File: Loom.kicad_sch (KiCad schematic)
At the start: 65 parts, among them SW1 SW_Push, SW2 SW_SPST, SW3 SW_Push, SW4 SW_Push

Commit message: Add wheel speed sensors, telemetry board
TODO:
- ETC
- Relay Indicator Board
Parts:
- added TEL1: Terminal Block, symbol Connector_Generic:Conn_01x02
- added TEL2: Amphenol AT, symbol Connector_Generic:Conn_01x02
- added WSF, WSR: TE AMPSEAL, symbol Connector_Generic:Conn_01x08
- added WSF1, WSF2, WSR1, WSR2: Conn_01x02, symbol Connector_Generic:Conn_01x02
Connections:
- net CANH: now also TEL2.1 (Pin_1), WSF.3 (Pin_3), WSR.3 (Pin_3)
- net CANL: now also TEL2.2 (Pin_2), WSF.2 (Pin_2), WSR.2 (Pin_2)
- net MiscPWR: now also TEL1.1 (Pin_1), WSF.1 (Pin_1), WSR.1 (Pin_1)
- net SENGND: now also TEL1.2 (Pin_2), WSF.8 (Pin_8), WSR.8 (Pin_8)
- new net: WSR.4 (Pin_4), WSR1.1 (Pin_1)
- new net: WSR.5 (Pin_5), WSR1.2 (Pin_2)
- new net: WSR.6 (Pin_6), WSR2.1 (Pin_1)
- new net: WSR.7 (Pin_7), WSR2.2 (Pin_2)
- new net: WSF.4 (Pin_4), WSF1.1 (Pin_1)
- new net: WSF.5 (Pin_5), WSF1.2 (Pin_2)
- new net: WSF.6 (Pin_6), WSF2.1 (Pin_1)
- new net: WSF.7 (Pin_7), WSF2.2 (Pin_2)
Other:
- note added: "(12V) Power CANL CANH Sens1S Sens1G Sens2S Sens2G Gnd"
- note added: "(12V) Power Ground"
- note added: "CANH CANL"
- note added: "Telemetry"
- note added: "Wheel Speed Sensors"
- moved on the sheet: D2, FAN1, FAN2, R1, R2, SW4

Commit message: Start splitting loom into separate front/rear
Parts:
- removed APP1, APP2, BPS: Conn_01x03, symbol Connector_Generic:Conn_01x03
- removed BLS: Conn_01x03, symbol Connector_Generic:Conn_01x02
- removed BSPD: AMPSEAL (776273-1), symbol Connector_Generic:Conn_01x14
- removed BTS, INS, WSF1, WSF2: Conn_01x02, symbol Connector_Generic:Conn_01x02
- removed D1, D2: LED_Small, symbol Device:LED_Small
- removed DSH1: TE 776273-1, symbol Connector_Generic:Conn_01x14
- removed DSH2: Superseal 1.5, Connector_PinHeader_2.54mm:PinHeader_1x06_P2.54mm_Vertical, symbol Connector_Generic:Conn_01x06
- removed DSH3: No Connector, symbol Connector_Generic:Conn_01x02
- removed DSH4: Superseal 1.5, symbol Connector_Generic:Conn_01x04
- removed DSH5: JST XH2.54, symbol Connector_Generic:Conn_01x04
- removed R1, R2: R_Small, symbol Device:R_Small
- removed SW1, SW3, SW4: SW_Push, symbol Switch:SW_Push
- removed SW2: SW_SPST, symbol Switch:SW_SPST
- removed TEL1: Terminal Block, symbol Connector_Generic:Conn_01x02
- removed TEL2: Amphenol AT, symbol Connector_Generic:Conn_01x02
- removed WSF: TE AMPSEAL, symbol Connector_Generic:Conn_01x08
- added TSP: Conn_01x04, symbol Connector_Generic:Conn_01x04
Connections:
- net MiscPWR: now also LES.1 (Pin_1)
- net Front of Firewall/BLSSig: now reaches BKL.2 (Pin_2)
- net Front of Firewall/TPSPwr1: now reaches TPS.1 (Pin_1)
- net Front of Firewall/TPSGnd1: now reaches TPS.3 (Pin_3)
- net Front of Firewall/TPSPwr2: now reaches TPS.4 (Pin_4)
- net Front of Firewall/TPSSig2: now reaches TPS.5 (Pin_5)
- net Front of Firewall/TPSGnd2: now reaches TPS.6 (Pin_6)
- new net Front of Firewall/STEP-1+: TSP.1 (Pin_1)
- new net Front of Firewall/STEP-1-: TSP.2 (Pin_2)
- new net Front of Firewall/STEP-2+: TSP.3 (Pin_3)
- new net Front of Firewall/STEP-2-: TSP.4 (Pin_4)
- no-connect marks 18 -> 10
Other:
- added sheet Front of Firewall (front.kicad_sch)
- note added: "Brake Light"
- note added: "Power Box (Distribution, Fuse and Relay Boxes, Starter Relay)"
- note added: "Throttle Body"
- note removed: "(12V) Power Ground"
- note removed: "(12V) Power Neutral Shift Dn Shift Up Tacho CANL CANH ESTOP 1 2 Starter Sig Fan Sig Gnd Gnd Gnd"
- note removed: "(12V) Power Signal"
- note removed: "(5V) Power Signal Ground"
- note removed: "Brake Sensors etc."
- note removed: "CANH CANL"
- note removed: "Dash Breakout PCB"
- note removed: "Dashboard"
- note removed: "Dashboard Left"
- note removed: "Dashboard Right"
- note removed: "Dashboard Screen"
- note removed: "Disp 5V TX RX Gnd"
- note removed: "ESTOP 1 2"
- note removed: "ETC Control"
- note removed: "Launch Control Button"
- note removed: "Neutral LED+ Neutral LED- Starter 12V Starter Sig Fan Sig Gnd"
- note removed: "Power (Battery, Fuse, LVMS, Distribution/Relay/Fuse Box)"
- note removed: "Power BPS Power BPS Signal BPS Ground Ground TPS Power TPS Signal TPS Ground Ground Shutdown C Shutdown NC Shutdown NO Ground Ground"
- note removed: "Power Signal Ground"
- note removed: "TODO Control Unit"
- note removed: "Telemetry"
- note removed: "to dash estop"
- company: (none) -> Full Blue Racing
- title: (none) -> FBR25 Loom - Electrical Diagram
- moved on the sheet: BAT, BKL, FSE, LES, LVM, QS1, QS2, QS3, QS4, QSS, RES, SER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

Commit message: Remove LVMSPwr, replace with MiscPwr
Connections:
- net MiscPWR: now also RBX4.85, RBX5.85
- net LVMS 12V: no longer names the net of DBX.1 (Pin_1), DBX.2 (Pin_2), DBX.3 (Pin_3), DBX.4 (Pin_4), DBX.5 (Pin_5), DBX.6 (Pin_6), DBX.7 (Pin_7), DBX.8 (Pin_8), FBX2.1 (Pin_1), FBX2.2 (Pin_2), FBX2.3 (Pin_3), FBX2.4 (Pin_4), FBX2.5 (Pin_5), LVM.2 (Pin_2), RBX1.87, RBX2.87, RBX3.87, RBX5.87
- net LVMS 12V: no longer RBX4.85, RBX5.85
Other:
- sheet Front of Firewall ports: added none; removed LVMSPWR
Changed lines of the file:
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@@
 	)
 	(junction
-		(at 553.72 149.86)
-		(diameter 0)
-		(color 0 0 0 0)
-	)
-	(junction
 		(at 223.52 233.68)
 		(diameter 0)
@@
 	)
 	(junction
-		(at 474.98 241.3)
+		(at 292.1 93.98)
 		(diameter 0)
-		(color 255 0 0 1)
+		(color 0 0 0 0)
 	)
 	(junction
-		(at 292.1 93.98)
+		(at 474.98 317.5)
 		(diameter 0)
 		(color 0 0 0 0)
@@
 	(wire
 		(pts
-			(xy 172.72 218.44) (xy 38.1 218.44)
-		)
-		(stroke
-			(width 0)
-			(type default)
-			(color 255 0 0 1)
-		)
-	)
-	(wire
-		(pts
 			(xy 165.1 274.32) (xy 38.1 274.32)
 		)
@@
 	(wire
 		(pts
-			(xy 474.98 259.08) (xy 474.98 307.34)
-		)
-		(stroke
-			(width 0)
-			(type default)
-			(color 255 0 0 1)
-		)
-	)
-	(wire
-		(pts
 			(xy 106.68 373.38) (xy 111.76 373.38)
 		)
@@
 	(wire
 		(pts
-			(xy 474.98 149.86) (xy 474.98 241.3)
-		)
-		(stroke
-			(width 0)
-			(type default)
-			(color 255 0 0 1)
-		)
-	)
-	(wire
-		(pts
 			(xy 248.92 299.72) (xy 248.92 223.52)
 		)
@@
 	(wire
 		(pts
-			(xy 373.38 317.5) (xy 541.02 317.5)
+			(xy 373.38 317.5) (xy 474.98 317.5)
 		)
 		(stroke
@@
 	(wire
 		(pts
+			(xy 474.98 317.5) (xy 541.02 317.5)
+		)
+		(stroke
+			(width 0)
+			(type default)
+			(color 255 0 0 1)
+		)
+	)
+	(wire
+		(pts
 			(xy 203.2 25.4) (xy 132.08 25.4)
 		)
@@
 	(wire
 		(pts
-			(xy 172.72 307.34) (xy 172.72 218.44)
-		)
-		(stroke
-			(width 0)
-			(type default)
-			(color 255 0 0 1)
-		)
-	)
-	(wire
-		(pts
 			(xy 429.26 22.86) (xy 538.48 22.86)
 		)
@@
 	(wire
 		(pts
-			(xy 474.98 149.86) (xy 553.72 149.86)
-		)
-		(stroke
-			(width 0)
-			(type default)
-			(color 255 0 0 1)
-		)
-	)
-	(wire
-		(pts
 			(xy 538.48 63.5) (xy 538.48 50.8)
 		)
@@
 	(wire
 		(pts
-			(xy 474.98 307.34) (xy 172.72 307.34)
+			(xy 236.22 330.2) (xy 152.4 330.2)
 		)
 		(stroke
 			(width 0)
 			(type default)
-			(color 255 0 0 1)
 		)
 	)
 	(wire
 		(pts
-			(xy 236.22 330.2) (xy 152.4 330.2)
+			(xy 474.98 259.08) (xy 474.98 317.5)
 		)
 		(stroke
 			(width 0)
 			(type default)
+			(color 255 0 0 1)
 		)
 	)
@@
 		)
 	)
-	(label "LVMS 12V"
-		(at 459.74 307.34 0)
-		(effects
-			(font
-				(size 1.27 1.27)
-			)
-			(justify left bottom)
-		)
-	)
 	(label "Starter_12V"
 		(at 490.22 86.36 0)
@@
 		)
 	)
-	(label "LVMS 12V"
-		(at 543.56 149.86 0)
-		(effects
-			(font
-				(size 1.27 1.27)
-				(thickness 0.1588)
-			)
-			(justify left bottom)
-		)
-	)
 	(label "CNK-"
 		(at 299.72 137.16 0)
@@
 			(effects
 				(font
-					(size 1.27 1.27)
-				)
-				(justify right)
-			)
-		)
-		(pin "LVMSPWR" input
-			(at 38.1 218.44 0)
-			(effects
-				(font

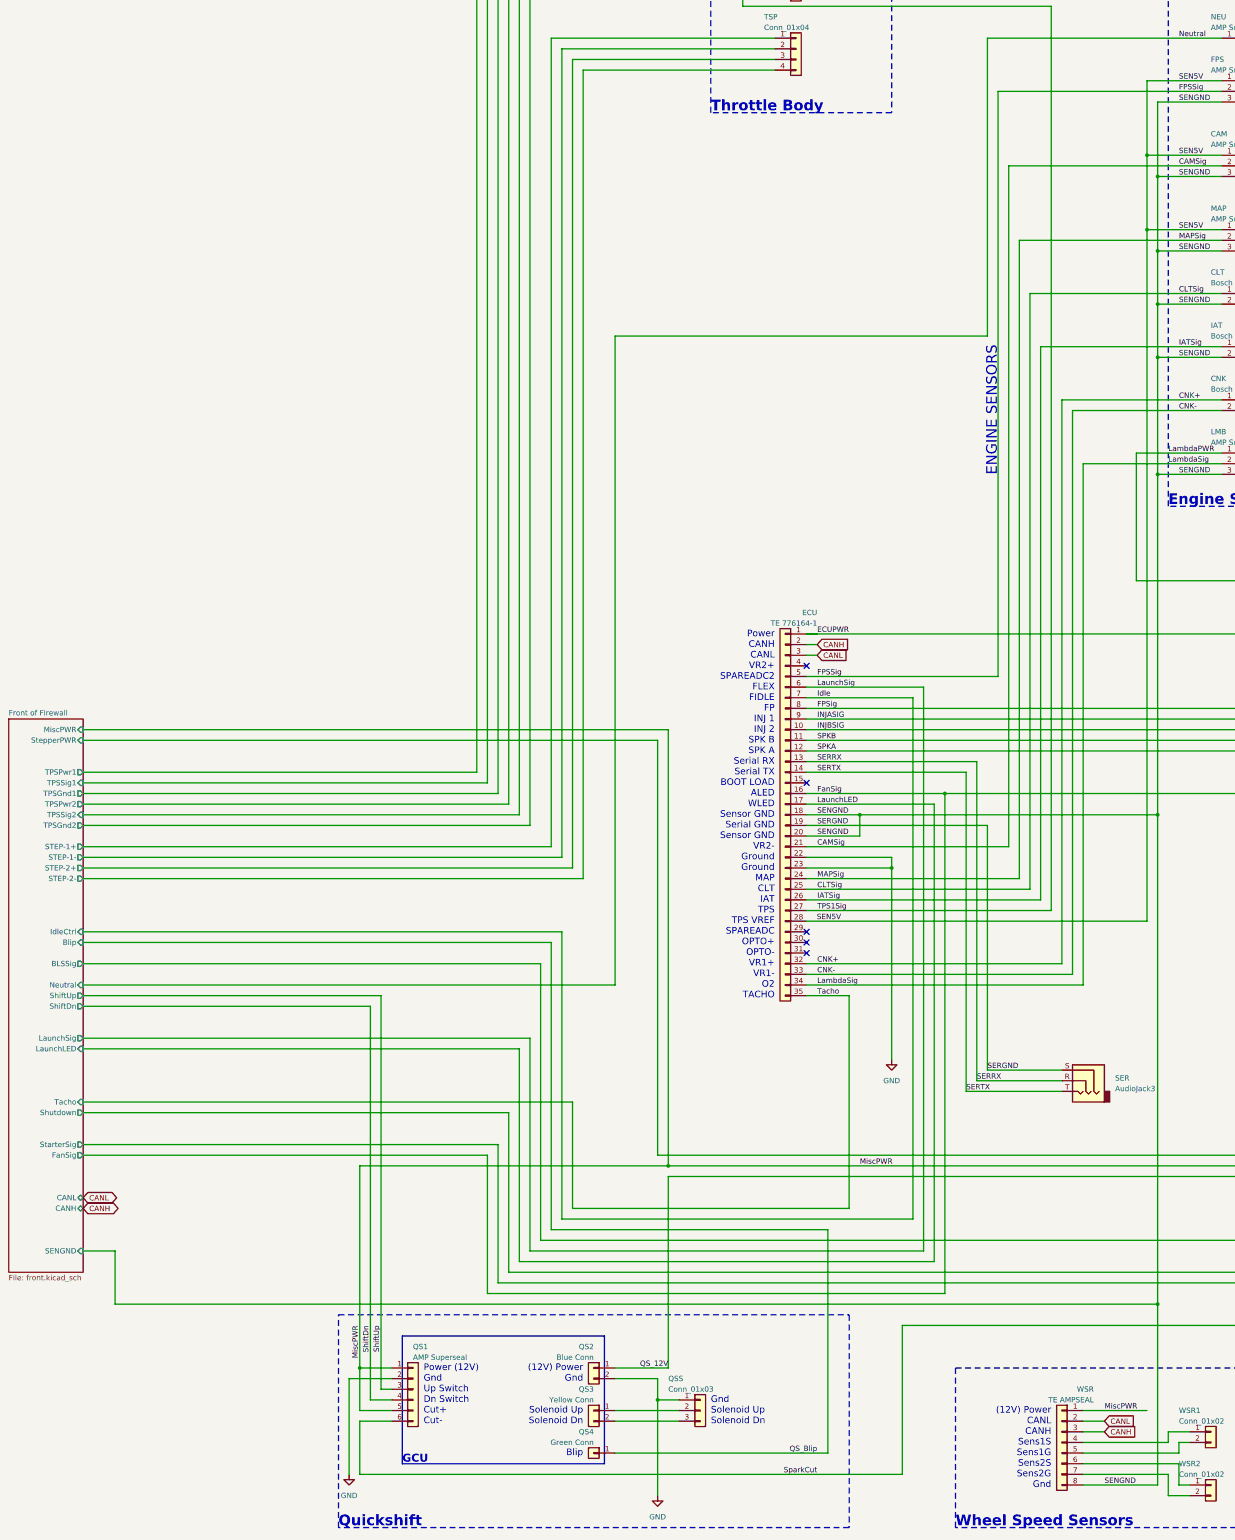
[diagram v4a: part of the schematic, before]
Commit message: Remove SENGND from front of loom
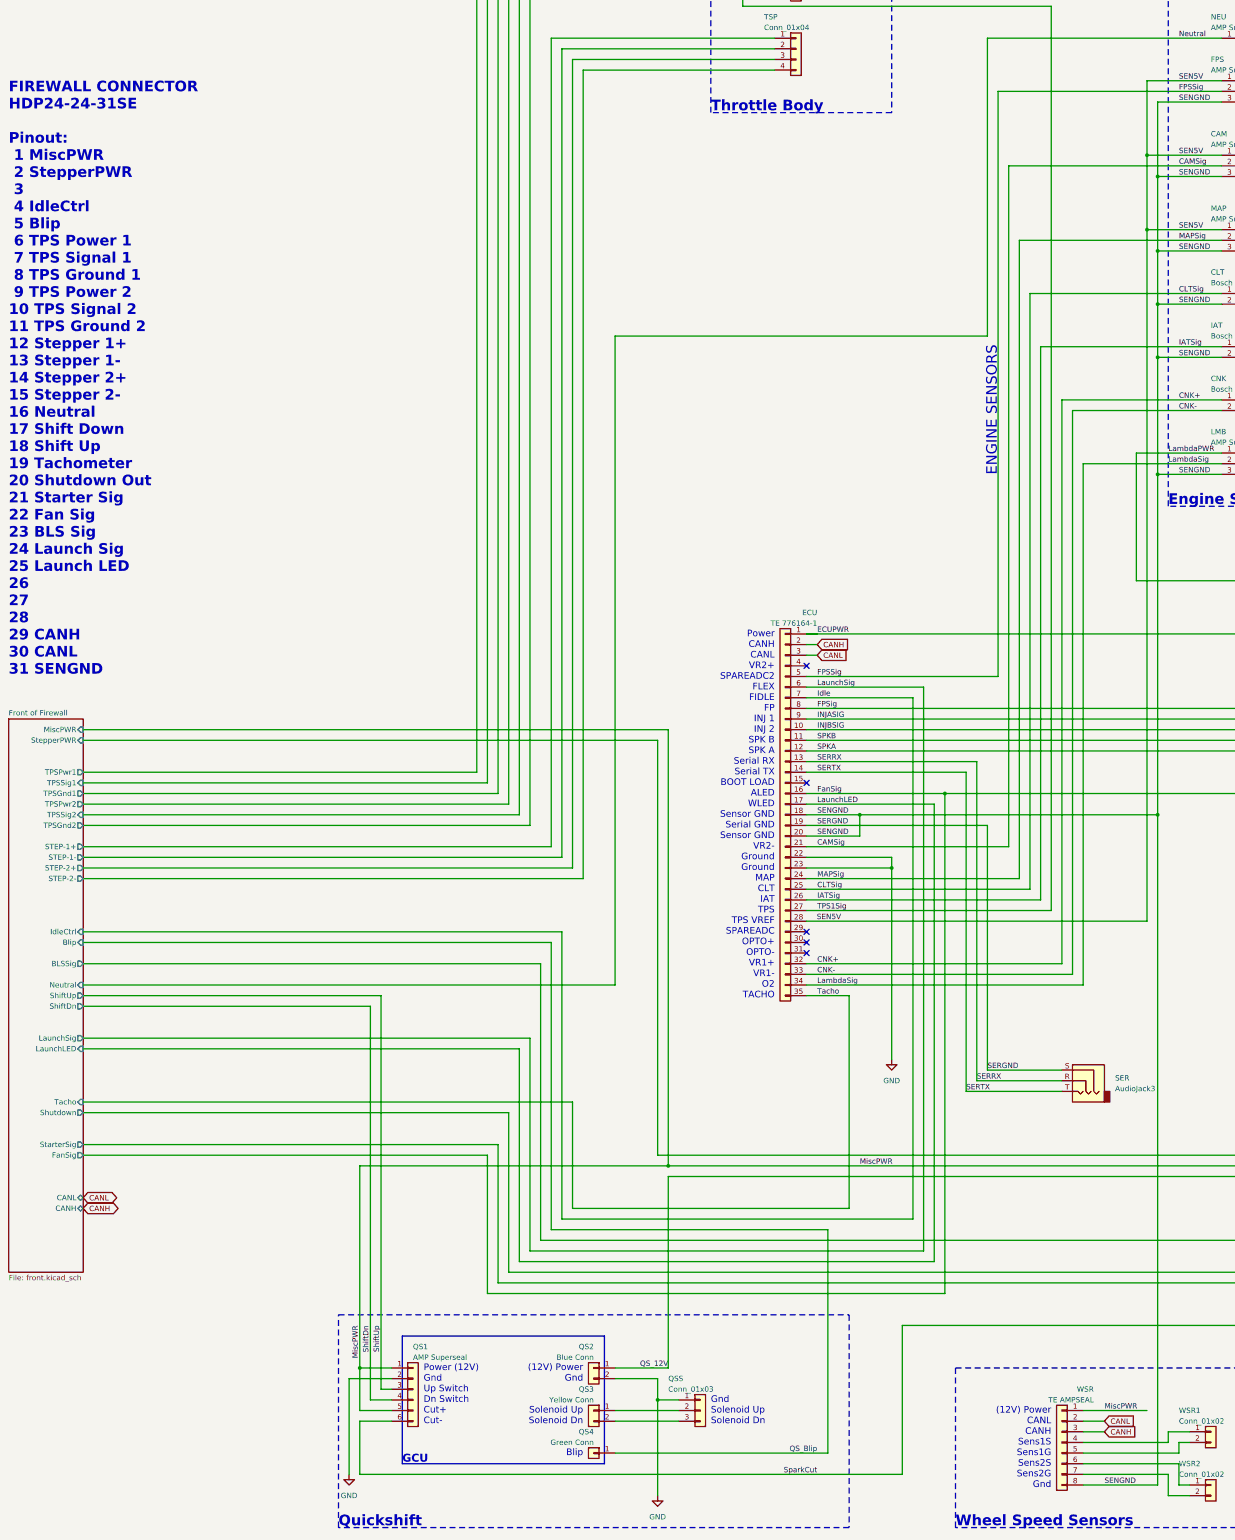
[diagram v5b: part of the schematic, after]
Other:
- sheet Front of Firewall ports: added none; removed SENGND
- note added: "FIREWALL CONNECTOR HDP24-24-31SE Pinout: 1 MiscPWR 2 StepperPWR 3 4 IdleCtrl 5 Blip 6 TPS Power 1 7 TPS Signal 1 8 TPS Ground 1 9 TPS Power 2 10 TPS Signal 2 11 TPS Ground 2 12 Stepper 1+ 13 Stepper 1- 14 Stepper 2+ 15 Stepper 2- 16 Neutral 17 Shift Down 18 Shift Up 19 Tachometer 20 Shutdown Out 21 Starter Sig 22 Fan Sig 23 BLS Sig 24 Launch Sig 25 Launch LED 26 27 28 29 CANH 30 CANL 31 SENGND"
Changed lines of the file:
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@@
 		)
 	)
+	(text "FIREWALL CONNECTOR\nHDP24-24-31SE\n\nPinout:\n 1 MiscPWR\n 2 StepperPWR\n 3 \n 4 IdleCtrl\n 5 Blip\n 6 TPS Power 1\n 7 TPS Signal 1\n 8 TPS Ground 1\n 9 TPS Power 2\n10 TPS Signal 2\n11 TPS Ground 2\n12 Stepper 1+\n13 Stepper 1-\n14 Stepper 2+\n15 Stepper 2-\n16 Neutral\n17 Shift Down\n18 Shift Up\n19 Tachometer\n20 Shutdown Out\n21 Starter Sig\n22 Fan Sig\n23 BLS Sig\n24 Launch Sig\n25 Launch LED\n26 \n27 \n28 \n29 CANH\n30 CANL\n31 SENGND"
+		(exclude_from_sim no)
+		(at 20.32 129.54 0)
+		(effects
+			(font
+				(size 2.54 2.54)
+				(thickness 0.508)
+				(bold yes)
+			)
+			(justify left)
+		)
+	)
 	(text "High\nLow"
 		(exclude_from_sim no)
@@
 	)
 	(junction
-		(at 294.64 350.52)
-		(diameter 0)
-		(color 0 0 0 0)
-	)
-	(junction
 		(at 474.98 259.08)
 		(diameter 0)
@@
 	(wire
 		(pts
-			(xy 45.72 337.82) (xy 45.72 350.52)
-		)
-		(stroke
-			(width 0)
-			(type default)
-			(color 0 0 64 1)
-		)
-	)
-	(wire
-		(pts
 			(xy 426.72 375.92) (xy 444.5 375.92)
 		)
@@
 	(wire
 		(pts
-			(xy 38.1 337.82) (xy 45.72 337.82)
-		)
-		(stroke
-			(width 0)
-			(type default)
-			(color 0 0 64 1)
-		)
-	)
-	(wire
-		(pts
 			(xy 276.86 383.54) (xy 297.18 383.54)
 		)
@@
 	(wire
 		(pts
-			(xy 45.72 350.52) (xy 294.64 350.52)
-		)
-		(stroke
-			(width 0)
-			(type default)
-			(color 0 0 64 1)
-		)
-	)
-	(wire
-		(pts
 			(xy 505.46 254) (xy 513.08 254)
 		)
@@
 	(wire
 		(pts
-			(xy 294.64 233.68) (xy 294.64 350.52)
-		)
-		(stroke
-			(width 0)
-			(type default)
-			(color 0 0 64 1)
-		)
-	)
-	(wire
-		(pts
 			(xy 195.58 27.94) (xy 203.2 27.94)
 		)
@@
 	(wire
 		(pts
-			(xy 294.64 350.52) (xy 294.64 393.7)
+			(xy 294.64 233.68) (xy 294.64 393.7)
 		)
 		(stroke
@@
 			(effects
 				(font
-					(size 1.27 1.27)
-				)
-				(justify right)
-			)
-		)
-		(pin "SENGND" input
-			(at 38.1 337.82 0)
-			(effects
-				(font

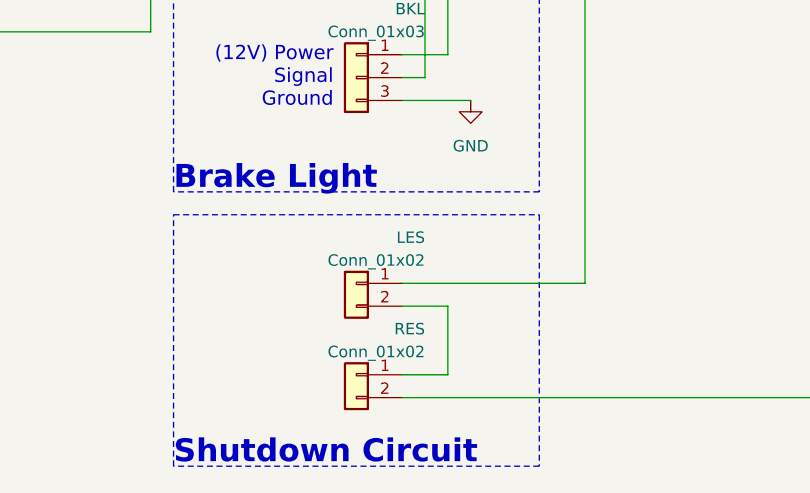
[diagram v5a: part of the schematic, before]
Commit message: swap LES/RES
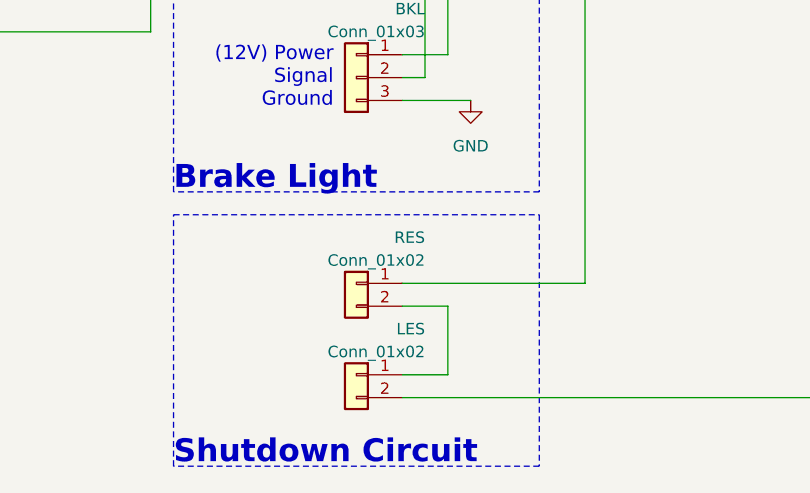
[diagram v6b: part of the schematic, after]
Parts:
- renumbered RES to LES, LES to RES
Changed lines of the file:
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@@
 		(on_board yes)
 		(dnp no)
-		(property "Reference" "LES"
+		(property "Reference" "RES"
 			(at 370.84 378.46 0)
 			(effects
@@
 			(project "Loom"
 				(path "/b6ef7529-600a-4e2f-9b83-5120e6f066ed"
-					(reference "LES")
+					(reference "RES")
 					(unit 1)
 				)
@@
 		(on_board yes)
 		(dnp no)
-		(property "Reference" "RES"
+		(property "Reference" "LES"
 			(at 370.84 388.62 0)
 			(effects
@@
 			(project "Loom"
 				(path "/b6ef7529-600a-4e2f-9b83-5120e6f066ed"
-					(reference "RES")
+					(reference "LES")
 					(unit 1)
 				)
